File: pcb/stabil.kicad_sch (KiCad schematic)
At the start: 44 parts, among them Q10 IRFR5305, U11 TPS5430DDA, U12 LM75B, U13 INA219AxD, U14 LM78M05_TO252, U16 TSV911IDT, U17 PC817

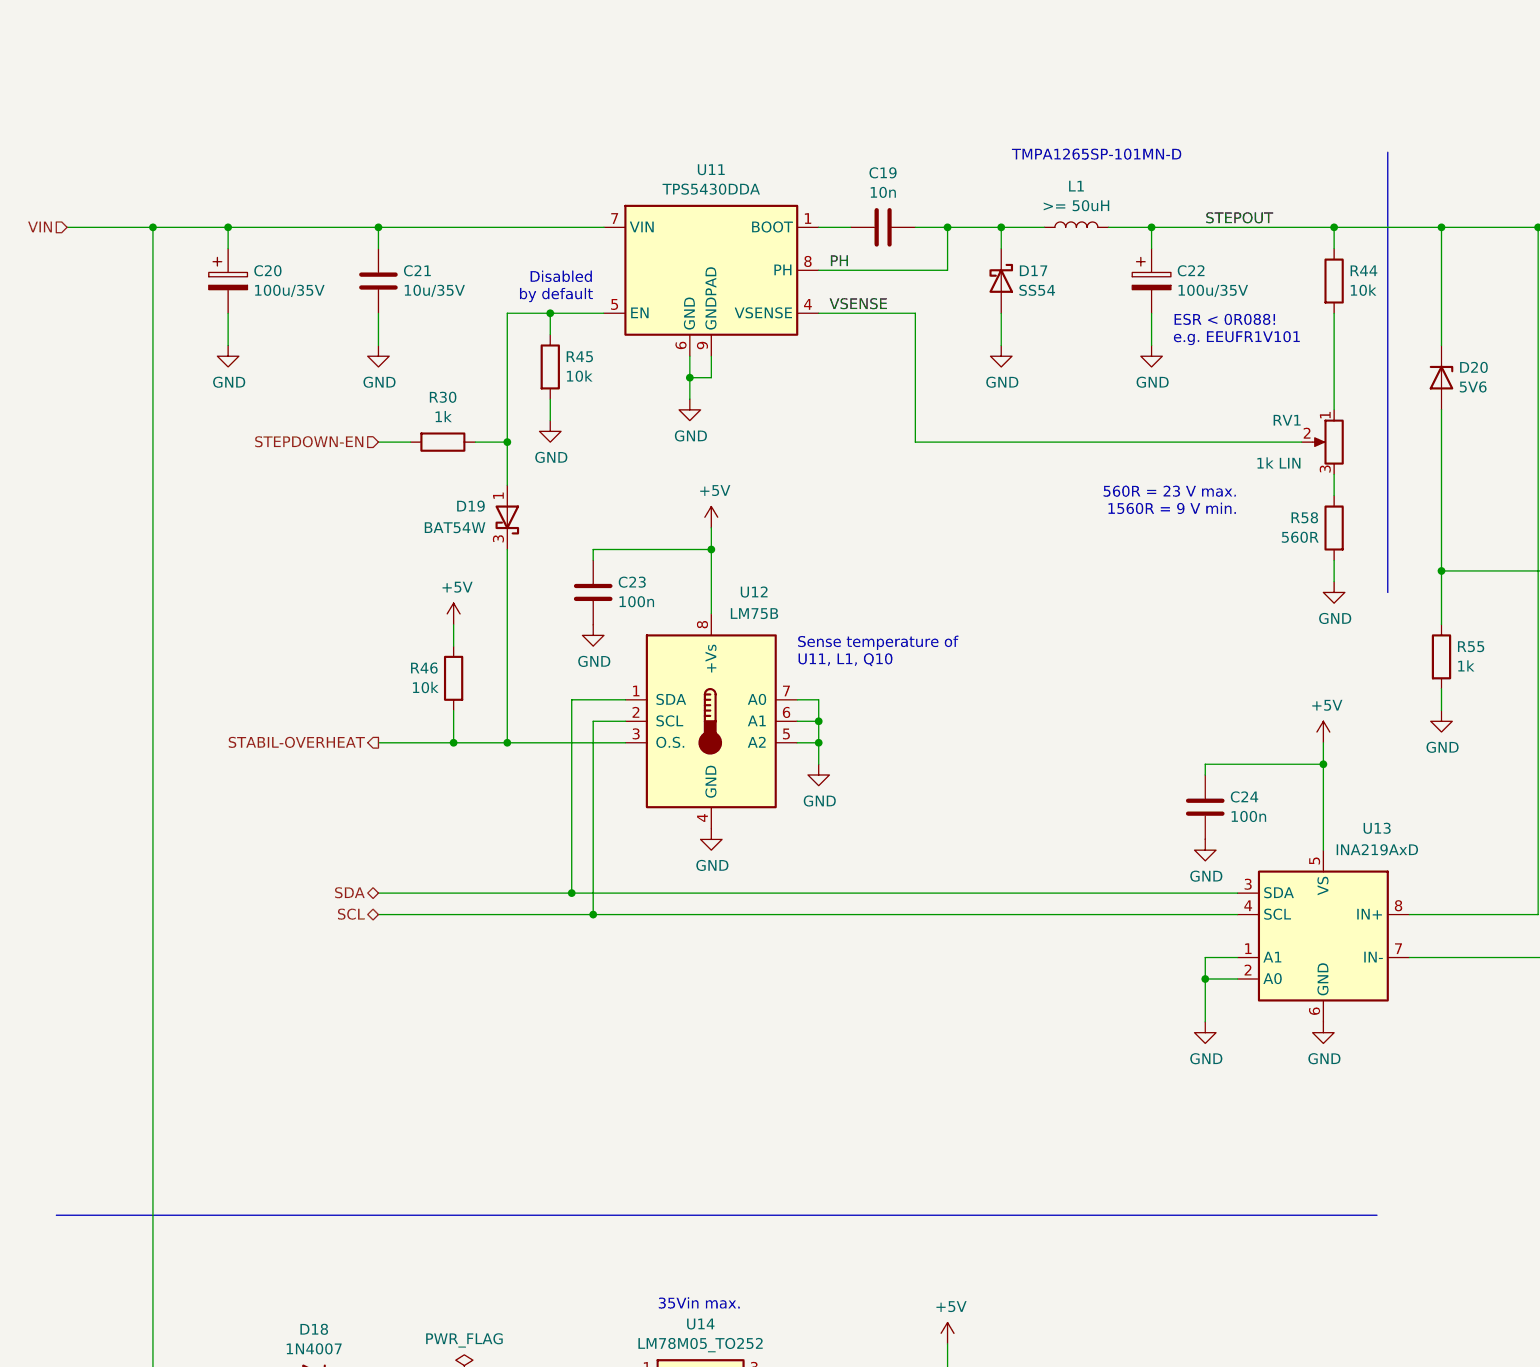
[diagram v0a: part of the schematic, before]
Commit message: Update to KiCad 8.
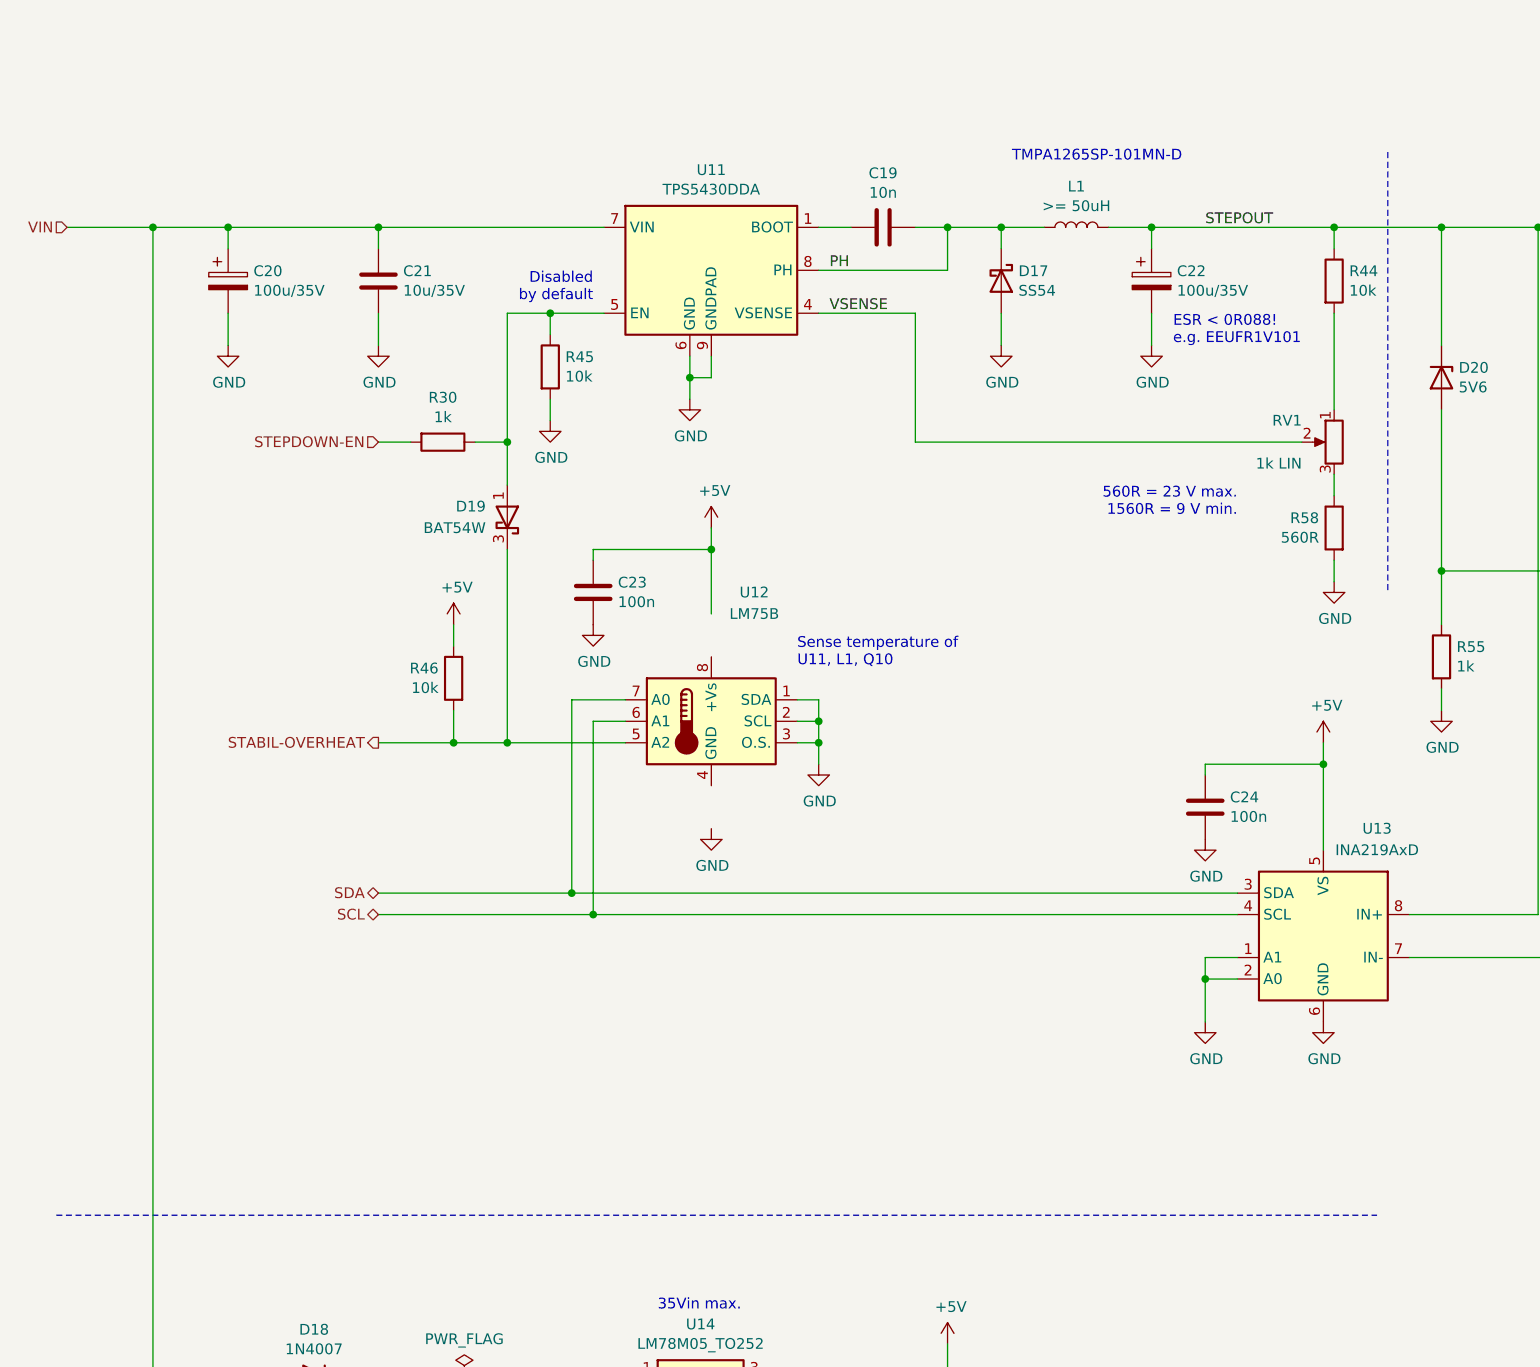
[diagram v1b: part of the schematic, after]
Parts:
- C20, C22, C25: symbol Device:CP -> Device:C_Polarized
- D19: footprint Package_TO_SOT_SMD:SOT-323_SC-70_Handsoldering -> Package_TO_SOT_SMD:SOT-323_SC-70
- D20, D?: footprint Diode_SMD:D_SOT-23_ANK -> Package_TO_SOT_SMD:SOT-23
- Q?: footprint Package_TO_SOT_SMD:SOT-223 -> Package_TO_SOT_THT:TO-92_Inline
- RV1, RV2: symbol Device:R_POT -> Device:R_Potentiometer
- U13: symbol Analog_ADC:INA219AxD -> Sensor_Energy:INA219AxD
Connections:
- net +5V: no longer U12.8 (+Vs)
- net GND: now also U12.1 (SDA), U12.2 (SCL), U12.3 (O.S.); no longer U12.4 (GND), U12.5 (A2), U12.6 (A1), U12.7 (A0)
- net SCL: now also U12.6 (A1); no longer U12.2 (SCL)
- net SDA: now also U12.7 (A0); no longer U12.1 (SDA)
- net STABIL-OVERHEAT: now also U12.5 (A2); no longer U12.3 (O.S.)
- net STEPOUT: now also D20.3 (K); no longer D20.1 (K)
- net at C14.2, C28.2, R53.1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: now also D20.1 (A); no longer D20.2 (A)
- net at C?.1, D?.1 (K), F?.2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: now also D?.3 (K); no longer D?.1 (K)
- net at C?.2, Q?.2 (G), R?.1: now also D?.1 (A); no longer D?.2 (A)

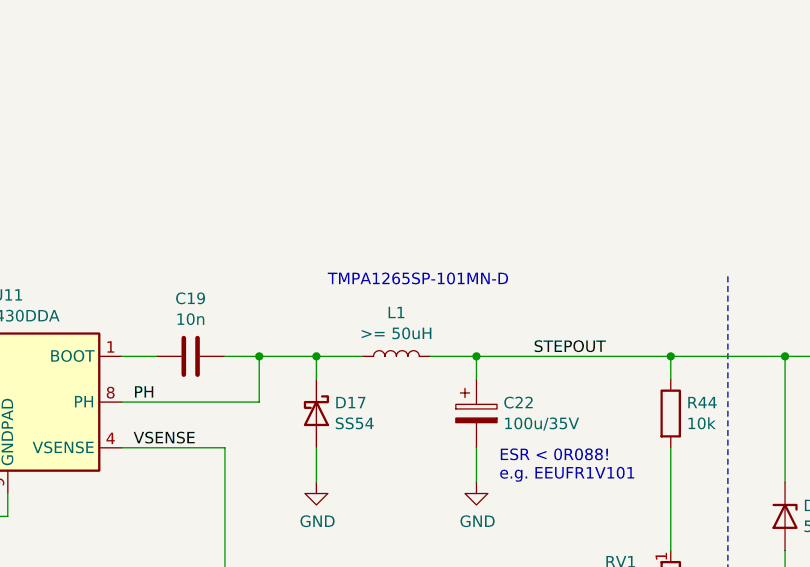
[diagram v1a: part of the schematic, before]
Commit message: Use 1N5819 instead of 1N4148.
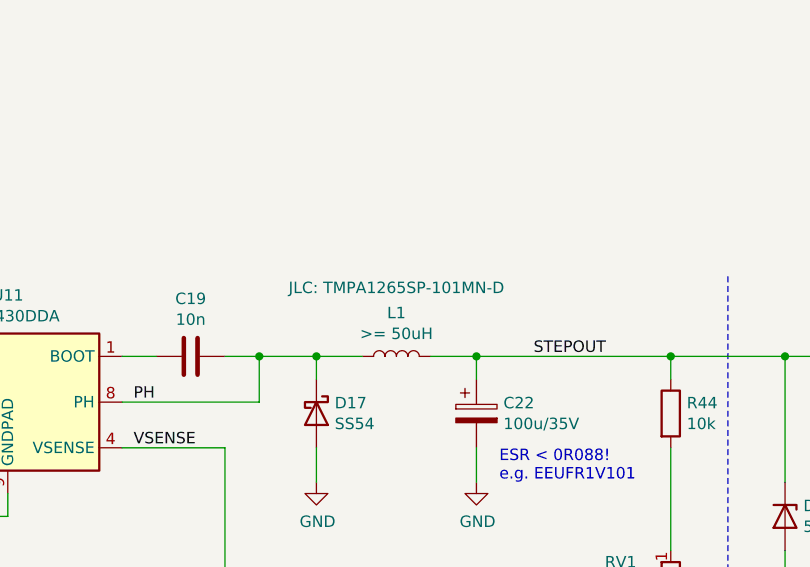
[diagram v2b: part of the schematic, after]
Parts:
- L1: JLC (none) -> TMPA1265SP-101MN-D
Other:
- note removed: "TMPA1265SP-101MN-D"
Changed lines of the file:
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@@
-		)
-	)
-	(text "TMPA1265SP-101MN-D"
-		(exclude_from_sim no)
-		(at 133.35 22.86 0)
-		(effects
-			(font
-				(size 1.27 1.27)
-			)
-			(justify left bottom)
 		)
 	)
@@
 			)
 		)
+		(property "JLC" "TMPA1265SP-101MN-D"
+			(at 140.97 22.86 90)
+			(show_name yes)
+			(effects
+				(font
+					(size 1.27 1.27)
+				)
+			)
+		)

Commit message: Export root page escription to other pages.
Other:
- company: (none) -> Model Railroader Club Brno I – KMŽ Brno I – https://kmz-brno.cz/
- title: HB22 – stabilization -> HB22 – DCC booster
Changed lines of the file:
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@@
 	(paper "A4")
 	(title_block
-		(title "HB22 – stabilization")
+		(title "HB22 – DCC booster")
+		(date "2025-02-20")
+		(rev "1.0")
+		(company "Model Railroader Club Brno I – KMŽ Brno I – https://kmz-brno.cz/")
+		(comment 1 "Jan Horáček")
+		(comment 2 "https://github.com/kmzbrnoI/hb22")
+		(comment 3 "https://creativecommons.org/licenses/by-sa/4.0/")
+		(comment 4 "Released under the Creative Commons Attribution-ShareAlike 4.0 License")
 	)
 	(junction

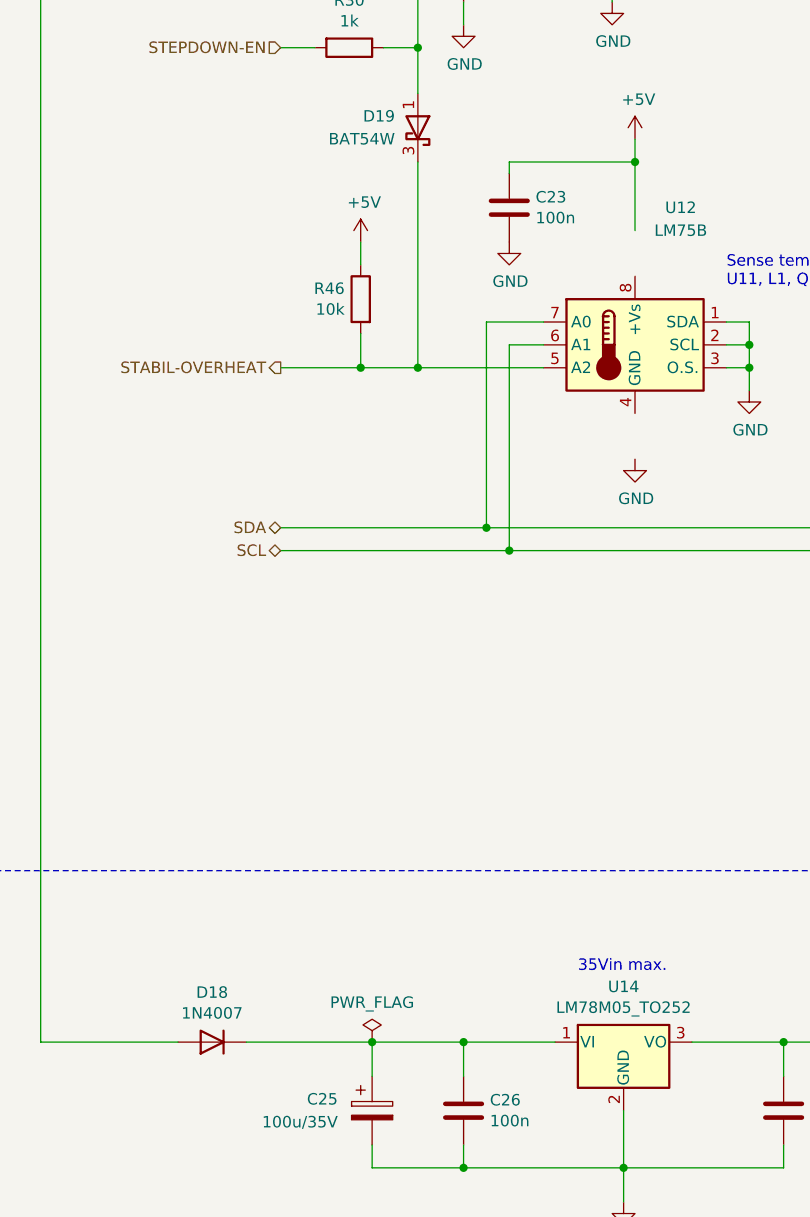
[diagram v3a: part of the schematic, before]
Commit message: Add capacitor to U7, fix new parts.
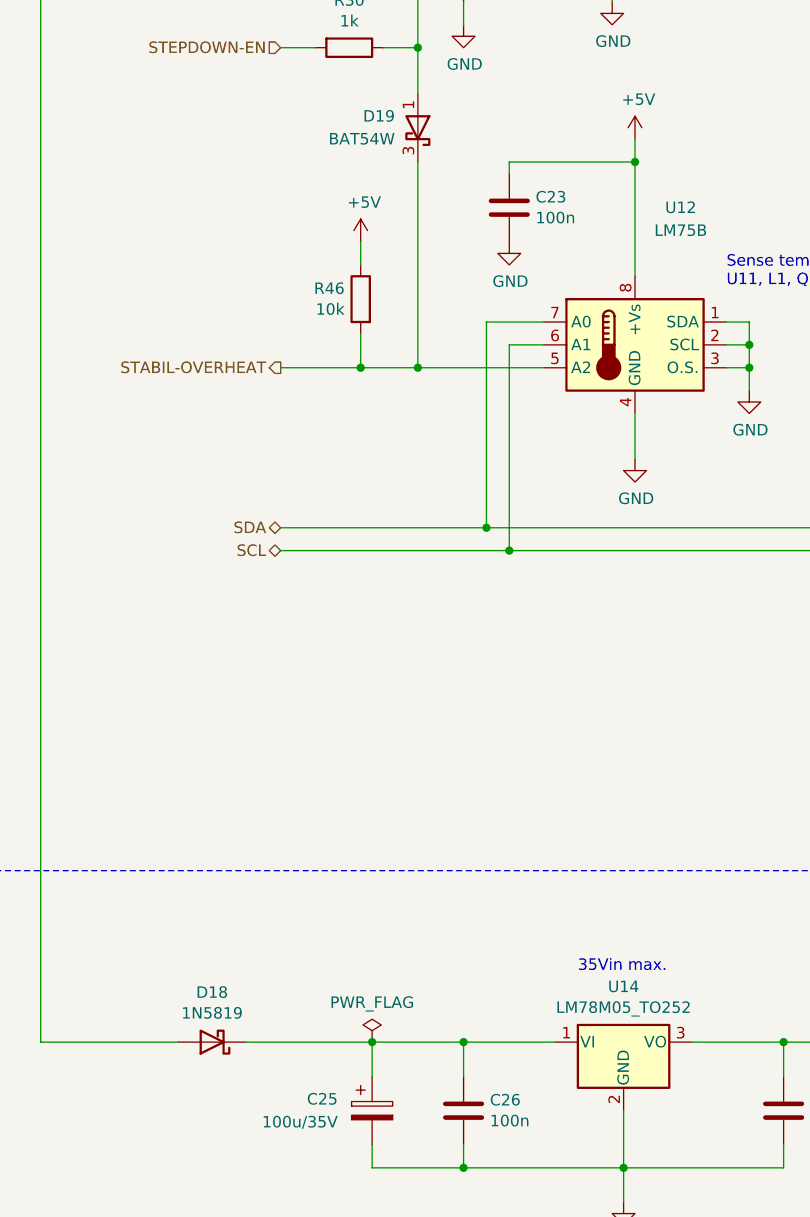
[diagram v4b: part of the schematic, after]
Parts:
- D18: value 1N4007 -> 1N5819; symbol Device:D -> Device:D_Schottky
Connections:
- net +5V: now also U12.8 (+Vs)
- net GND: now also U12.4 (GND)
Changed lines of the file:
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@@
+	(wire
+		(pts
+			(xy 97.79 96.52) (xy 97.79 101.6)
+		)
+		(stroke
+			(width 0)
+			(type default)
+		)
+	)
 	(wire
 		(pts
@@
 	(wire
 		(pts
-			(xy 97.79 76.2) (xy 97.79 68.58)
+			(xy 97.79 68.58) (xy 97.79 81.28)
 		)
 		(stroke
@@
 	)
 	(symbol
-		(lib_id "Device:D")
+		(lib_id "Device:D_Schottky")
 		(at 50.8 166.37 180)
 		(unit 1)
@@
 			)
 		)
-		(property "Value" "1N4007"
+		(property "Value" "1N5819"
 			(at 50.8 163.1696 0)
 			(effects
@@
 			)
 		)
-		(property "Description" "Diode"
+		(property "Description" "Schottky diode"
 			(at 50.8 166.37 0)
 			(effects
